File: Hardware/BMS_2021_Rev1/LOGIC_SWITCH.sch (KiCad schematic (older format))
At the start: 0 parts

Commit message: done (need to do LEDs)
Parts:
- added D?: 3V3_Zener, symbol Device:D_Zener
- added F?: Polyfuse, symbol Device:Polyfuse
- added Q?: 2N7000, Package_TO_SOT_THT:TO-92_Inline, symbol Transistor_FET:2N7000
- added R?: 10k, symbol Device:R
- added R?: 1.01M, symbol Device:R
- added R?: 110k, symbol Device:R
- added SW?: Relay_SPST, symbol MRDT_Switches:Relay_SPST
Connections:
- net labels added: +5V, GND, PV, logic_power, logic_power_sense, logic_switch
- wire segments 0 -> 25
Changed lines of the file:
@@
 $Descr A 11000 8500
 encoding utf-8
-Sheet 7 10
+Sheet 11 11
 Title ""
 Date ""
@@
 Comment4 ""
 $EndDescr
+Text HLabel 1650 2400 0    50   Input ~ 0
+logic_switch
+Wire Wire Line
+	1650 2400 1700 2400
+Wire Wire Line
+	1700 2400 1700 2750
+Connection ~ 1700 2400
+Wire Wire Line
+	1700 2400 2000 2400
+$Comp
+L Transistor_FET:2N7000 Q?
+U 1 1 5F8BB77C
+P 2200 2400
+F 0 "Q?" H 2404 2446 50  0000 L CNN
+F 1 "2N7000" H 2404 2355 50  0000 L CNN
+F 2 "Package_TO_SOT_THT:TO-92_Inline" H 2400 2325 50  0001 L CIN
+F 3 "https://www.fairchildsemi.com/datasheets/2N/2N7000.pdf" H 2200 2400 50  0001 L CNN
+	1    2200 2400
+	1    0    0    -1
+$EndComp
+Wire Wire Line
+	2300 2600 2300 2750
+Wire Wire Line
+	1700 2750 1800 2750
+$Comp
+L Device:R R?
+U 1 1 5F8BD0E6
+P 1950 2750
+F 0 "R?" V 1850 2750 50  0000 C CNN
+F 1 "10k" V 1950 2750 39  0000 C CNN
+F 2 "" V 1880 2750 50  0001 C CNN
+F 3 "~" H 1950 2750 50  0001 C CNN
+	1    1950 2750
+	0    1    1    0
+$EndComp
+Wire Wire Line
+	2100 2750 2300 2750
+$Comp
+L power:GND #PWR?
+U 1 1 5F8BD9DB
+P 2300 2850
+F 0 "#PWR?" H 2300 2600 50  0001 C CNN
+F 1 "GND" H 2305 2677 50  0000 C CNN
+F 2 "" H 2300 2850 50  0001 C CNN
+F 3 "" H 2300 2850 50  0001 C CNN
+	1    2300 2850
+	1    0    0    -1
+$EndComp
+Wire Wire Line
+	2300 2750 2300 2850
+Connection ~ 2300 2750
+$Comp
+L MRDT_Switches:Relay_SPST SW?
+U 1 1 5F8BE4C1
+P 2250 1650
+F 0 "SW?" H 2828 1788 50  0000 L CNN
+F 1 "Relay_SPST" H 2828 1697 50  0000 L CNN
+F 2 "" H 2500 2050 50  0001 C CNN
+F 3 "" H 2500 2050 50  0001 C CNN
+	1    2250 1650
+	1    0    0    -1
+$EndComp
+$Comp
+L power:+5V #PWR?
+U 1 1 5F8C0147
+P 2450 1900
+F 0 "#PWR?" H 2450 1750 50  0001 C CNN
+F 1 "+5V" H 2465 2073 50  0000 C CNN
+F 2 "" H 2450 1900 50  0001 C CNN
+F 3 "" H 2450 1900 50  0001 C CNN
+	1    2450 1900
+	-1   0    0    1
+$EndComp
+Wire Wire Line
+	2450 1900 2450 1750
+Wire Wire Line
+	2300 1750 2300 2200
+Wire Wire Line
+	2600 1750 2600 1850
+Text HLabel 2600 1850 3    50   Input ~ 0
+PV
+Wire Wire Line
+	2750 1750 2750 1850
+Wire Wire Line
+	2750 1850 3100 1850
+$Comp
+L Device:Polyfuse F?
+U 1 1 5F8C10D5
+P 3250 1850
+F 0 "F?" V 3450 1850 50  0000 C CNN
+F 1 "Polyfuse" V 3350 1850 50  0000 C CNN
+F 2 "" H 3300 1650 50  0001 L CNN
+F 3 "~" H 3250 1850 50  0001 C CNN
+	1    3250 1850
+	0    1    1    0
+$EndComp
+Wire Wire Line
+	3400 1850 3650 1850
+Wire Wire Line
+	3900 1850 3900 1750
+Wire Wire Line
+	3900 1750 3950 1750
+Text HLabel 3950 1750 2    50   Output ~ 0
+logic_power
+$Comp
+L Device:R R?
+U 1 1 5F8C18A1
+P 3650 2050
+F 0 "R?" H 3720 2088 50  0000 L CNN
+F 1 "1.01M" V 3650 1955 39  0000 L CNN
+F 2 "" V 3580 2050 50  0001 C CNN
+F 3 "~" H 3650 2050 50  0001 C CNN
+	1    3650 2050
+	1    0    0    -1
+$EndComp
+$Comp
+L Device:R R?
+U 1 1 5F8C1C00
+P 3650 2550
+F 0 "R?" H 3720 2588 50  0000 L CNN
+F 1 "110k" V 3645 2485 39  0000 L CNN
+F 2 "" V 3580 2550 50  0001 C CNN
+F 3 "~" H 3650 2550 50  0001 C CNN
+	1    3650 2550
+	1    0    0    -1
+$EndComp
+Connection ~ 3100 1850
+Wire Wire Line
+	3100 1850 3350 1850
+Wire Wire Line
+	3650 1900 3650 1850
+Connection ~ 3650 1850
+Wire Wire Line
+	3650 1850 3900 1850
+Wire Wire Line
+	3650 2200 3650 2300
+Wire Wire Line
+	3650 2700 3650 2800
+Wire Wire Line
+	3650 2300 3850 2300
+Connection ~ 3650 2300
+Wire Wire Line
+	3650 2300 3650 2400
+Text HLabel 3850 2300 2    50   Output ~ 0
+logic_power_sense
+$Comp
+L power:GND #PWR?
+U 1 1 5F8C3759
+P 3650 2800
+F 0 "#PWR?" H 3650 2550 50  0001 C CNN
+F 1 "GND" H 3655 2627 50  0000 C CNN
+F 2 "" H 3650 2800 50  0001 C CNN
+F 3 "" H 3650 2800 50  0001 C CNN
+	1    3650 2800
+	1    0    0    -1
+$EndComp
+$Comp
+L Device:D_Zener D?
+U 1 1 5F8C4713
+P 3350 2300
+F 0 "D?" H 3350 2500 50  0000 C CNN
+F 1 "3V3_Zener" H 3400 2400 50  0000 C CNN
+F 2 "" H 3350 2300 50  0001 C CNN
+F 3 "~" H 3350 2300 50  0001 C CNN
+	1    3350 2300
+	-1   0    0    1
+$EndComp
+Wire Wire Line
+	3500 2300 3650 2300
+Wire Wire Line
+	3200 2300 3000 2300
+Wire Wire Line
+	3000 2300 3000 2500
+$Comp
+L power:GND #PWR?
+U 1 1 5F8C556A
+P 3000 2500
+F 0 "#PWR?" H 3000 2250 50  0001 C CNN
+F 1 "GND" H 3005 2327 50  0000 C CNN
+F 2 "" H 3000 2500 50  0001 C CNN
+F 3 "" H 3000 2500 50  0001 C CNN
+	1    3000 2500
+	1    0    0    -1
+$EndComp
 $EndSCHEMATC

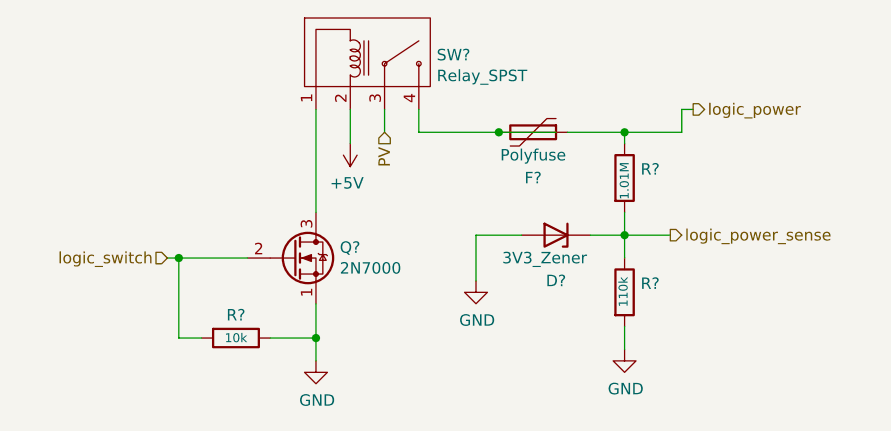
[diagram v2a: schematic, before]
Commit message: notes from PDR made. to be fixed
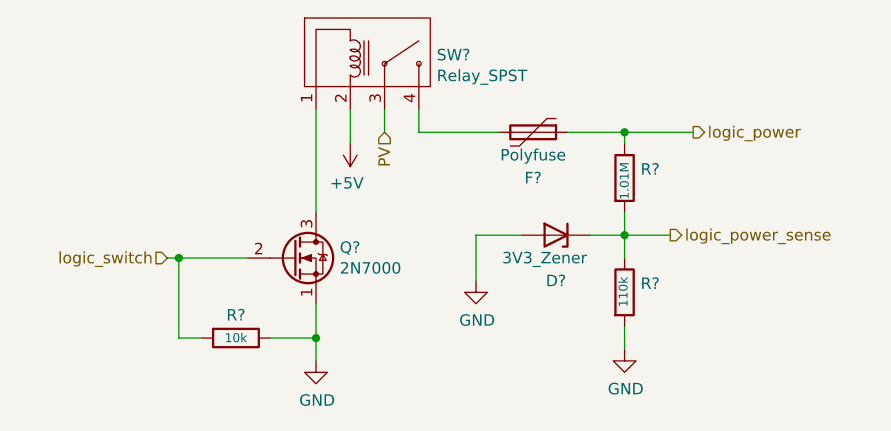
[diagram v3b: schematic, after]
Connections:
- wire segments 25 -> 22
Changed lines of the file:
@@
 $Descr A 11000 8500
 encoding utf-8
-Sheet 11 11
+Sheet 10 11
 Title ""
 Date ""
@@
 Wire Wire Line
 	3400 1850 3650 1850
-Wire Wire Line
-	3900 1850 3900 1750
-Wire Wire Line
-	3900 1750 3950 1750
-Text HLabel 3950 1750 2    50   Output ~ 0
-logic_power
 $Comp
 L Device:R R?
@@
 	1    0    0    -1
 $EndComp
-Connection ~ 3100 1850
-Wire Wire Line
-	3100 1850 3350 1850
 Wire Wire Line
 	3650 1900 3650 1850
 Connection ~ 3650 1850
-Wire Wire Line
-	3650 1850 3900 1850
 Wire Wire Line
 	3650 2200 3650 2300
@@
 	1    0    0    -1
 $EndComp
+Text HLabel 3950 1850 2    50   Output ~ 0
+logic_power
+Wire Wire Line
+	3650 1850 3950 1850
 $EndSCHEMATC

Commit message: annotated sch.
some ICs got moved around- solve later
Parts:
- gave numbers to parts that had none: 7
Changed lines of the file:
@@
 	1700 2400 2000 2400
 $Comp
-L Transistor_FET:2N7000 Q?
+L Transistor_FET:2N7000 Q4
 U 1 1 5F8BB77C
 P 2200 2400
-F 0 "Q?" H 2404 2446 50  0000 L CNN
+F 0 "Q4" H 2404 2446 50  0000 L CNN
 F 1 "2N7000" H 2404 2355 50  0000 L CNN
 F 2 "Package_TO_SOT_THT:TO-92_Inline" H 2400 2325 50  0001 L CIN
@@
 	1700 2750 1800 2750
 $Comp
-L Device:R R?
+L Device:R R44
 U 1 1 5F8BD0E6
 P 1950 2750
-F 0 "R?" V 1850 2750 50  0000 C CNN
+F 0 "R44" V 1850 2750 50  0000 C CNN
 F 1 "10k" V 1950 2750 39  0000 C CNN
 F 2 "" V 1880 2750 50  0001 C CNN
@@
 	2100 2750 2300 2750
 $Comp
-L power:GND #PWR?
+L power:GND #PWR055
 U 1 1 5F8BD9DB
 P 2300 2850
-F 0 "#PWR?" H 2300 2600 50  0001 C CNN
+F 0 "#PWR055" H 2300 2600 50  0001 C CNN
 F 1 "GND" H 2305 2677 50  0000 C CNN
 F 2 "" H 2300 2850 50  0001 C CNN
@@
 Connection ~ 2300 2750
 $Comp
-L MRDT_Switches:Relay_SPST SW?
+L MRDT_Switches:Relay_SPST SW1
 U 1 1 5F8BE4C1
 P 2250 1650
-F 0 "SW?" H 2828 1788 50  0000 L CNN
+F 0 "SW1" H 2828 1788 50  0000 L CNN
 F 1 "Relay_SPST" H 2828 1697 50  0000 L CNN
 F 2 "" H 2500 2050 50  0001 C CNN
@@
 $EndComp
 $Comp
-L power:+5V #PWR?
+L power:+5V #PWR056
 U 1 1 5F8C0147
 P 2450 1900
-F 0 "#PWR?" H 2450 1750 50  0001 C CNN
+F 0 "#PWR056" H 2450 1750 50  0001 C CNN
 F 1 "+5V" H 2465 2073 50  0000 C CNN
 F 2 "" H 2450 1900 50  0001 C CNN
@@
 	2750 1850 3100 1850
 $Comp
-L Device:Polyfuse F?
+L Device:Polyfuse F1
 U 1 1 5F8C10D5
 P 3250 1850
-F 0 "F?" V 3450 1850 50  0000 C CNN
+F 0 "F1" V 3450 1850 50  0000 C CNN
 F 1 "Polyfuse" V 3350 1850 50  0000 C CNN
 F 2 "" H 3300 1650 50  0001 L CNN
@@
 	3400 1850 3650 1850
 $Comp
-L Device:R R?
+L Device:R R45
 U 1 1 5F8C18A1
 P 3650 2050
-F 0 "R?" H 3720 2088 50  0000 L CNN
+F 0 "R45" H 3720 2088 50  0000 L CNN
 F 1 "1.01M" V 3650 1955 39  0000 L CNN
 F 2 "" V 3580 2050 50  0001 C CNN
@@
 $EndComp
 $Comp
-L Device:R R?
+L Device:R R46
 U 1 1 5F8C1C00
 P 3650 2550
-F 0 "R?" H 3720 2588 50  0000 L CNN
+F 0 "R46" H 3720 2588 50  0000 L CNN
 F 1 "110k" V 3645 2485 39  0000 L CNN
 F 2 "" V 3580 2550 50  0001 C CNN
@@
 logic_power_sense
 $Comp
-L power:GND #PWR?
+L power:GND #PWR058
 U 1 1 5F8C3759
 P 3650 2800
-F 0 "#PWR?" H 3650 2550 50  0001 C CNN
+F 0 "#PWR058" H 3650 2550 50  0001 C CNN
 F 1 "GND" H 3655 2627 50  0000 C CNN
 F 2 "" H 3650 2800 50  0001 C CNN
@@
 $EndComp
 $Comp
-L Device:D_Zener D?
+L Device:D_Zener D20
 U 1 1 5F8C4713
 P 3350 2300
-F 0 "D?" H 3350 2500 50  0000 C CNN
+F 0 "D20" H 3350 2500 50  0000 C CNN
 F 1 "3V3_Zener" H 3400 2400 50  0000 C CNN
 F 2 "" H 3350 2300 50  0001 C CNN
@@
 	3000 2300 3000 2500
 $Comp
-L power:GND #PWR?
+L power:GND #PWR057
 U 1 1 5F8C556A
 P 3000 2500
-F 0 "#PWR?" H 3000 2250 50  0001 C CNN
+F 0 "#PWR057" H 3000 2250 50  0001 C CNN
 F 1 "GND" H 3005 2327 50  0000 C CNN
 F 2 "" H 3000 2500 50  0001 C CNN

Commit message: Began assigning footprints
Downloaded some footprint files from UltraLibrarian. Put in BMS_Hardware>Documentation> then copied files where they need to go
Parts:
- F1: footprint (none) -> Fuse:Fuse_2920_7451Metric
- SW1: footprint (none) -> MRDT_Connectors:MOLEX_SL_04_Vertical
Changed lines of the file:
@@
 F 0 "SW1" H 2828 1788 50  0000 L CNN
 F 1 "Relay_SPST" H 2828 1697 50  0000 L CNN
-F 2 "" H 2500 2050 50  0001 C CNN
+F 2 "MRDT_Connectors:MOLEX_SL_04_Vertical" H 2500 2050 50  0001 C CNN
 F 3 "" H 2500 2050 50  0001 C CNN
 	1    2250 1650
@@
 F 0 "F1" V 3450 1850 50  0000 C CNN
 F 1 "Polyfuse" V 3350 1850 50  0000 C CNN
-F 2 "" H 3300 1650 50  0001 L CNN
+F 2 "Fuse:Fuse_2920_7451Metric" H 3300 1650 50  0001 L CNN
 F 3 "~" H 3250 1850 50  0001 C CNN
 	1    3250 1850

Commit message: more footprints added
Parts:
- R44, R45, R46: footprint (none) -> Resistor_SMD:R_0603_1608Metric_Pad1.05x0.95mm_HandSolder
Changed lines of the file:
@@
 F 0 "R44" V 1850 2750 50  0000 C CNN
 F 1 "10k" V 1950 2750 39  0000 C CNN
-F 2 "" V 1880 2750 50  0001 C CNN
+F 2 "Resistor_SMD:R_0603_1608Metric_Pad1.05x0.95mm_HandSolder" V 1880 2750 50  0001 C CNN
 F 3 "~" H 1950 2750 50  0001 C CNN
 	1    1950 2750
@@
 F 0 "R45" H 3720 2088 50  0000 L CNN
 F 1 "1.01M" V 3650 1955 39  0000 L CNN
-F 2 "" V 3580 2050 50  0001 C CNN
+F 2 "Resistor_SMD:R_0603_1608Metric_Pad1.05x0.95mm_HandSolder" V 3580 2050 50  0001 C CNN
 F 3 "~" H 3650 2050 50  0001 C CNN
 	1    3650 2050
@@
 F 0 "R46" H 3720 2588 50  0000 L CNN
 F 1 "110k" V 3645 2485 39  0000 L CNN
-F 2 "" V 3580 2550 50  0001 C CNN
+F 2 "Resistor_SMD:R_0603_1608Metric_Pad1.05x0.95mm_HandSolder" V 3580 2550 50  0001 C CNN
 F 3 "~" H 3650 2550 50  0001 C CNN
 	1    3650 2550

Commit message: Layout generated v1
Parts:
- D20: footprint (none) -> Diode_SMD:D_0603_1608Metric_Pad1.05x0.95mm_HandSolder
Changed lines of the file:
@@
 F 0 "D20" H 3350 2500 50  0000 C CNN
 F 1 "3V3_Zener" H 3400 2400 50  0000 C CNN
-F 2 "" H 3350 2300 50  0001 C CNN
+F 2 "Diode_SMD:D_0603_1608Metric_Pad1.05x0.95mm_HandSolder" H 3350 2300 50  0001 C CNN
 F 3 "~" H 3350 2300 50  0001 C CNN
 	1    3350 2300
